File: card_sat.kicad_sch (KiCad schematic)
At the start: 24 parts, among them J1 Conn_01x05_Male, J2 Conn_01x05_Male, J3 Conn_01x05_Male, J4 Conn_01x05_Male, J5 Conn_01x04_Male, U1 ATtiny85-20P, U2 ATtiny85-20P, U3 ATtiny85-20P

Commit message: changed schematic to use pico
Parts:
- removed D1, D2: B340, symbol Diode:B340
- removed R10, R11: (no value), symbol Device:R
- removed U1, U2, U3: ATtiny85-20P, Package_DIP:DIP-8_W7.62mm, symbol MCU_Microchip_ATtiny:ATtiny85-20P
- added D1, D2: (no value), symbol Diode:1N5819
- added U1: (no value), symbol MCU_RaspberryPi_and_Boards:Pico
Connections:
- net +3V3: now also U1.36 (3V3)
- net +5V: now also D1.1 (K), D2.1 (K)
- net GND: now also U1.38 (GND)
- net PANEL1: now also D1.2 (A)
- net PANEL2: now also D2.2 (A)
- net RXD1: now also U1.4 (GPIO2); no longer J1.2 (Pin_2), J2.2 (Pin_2)
- net RXD2: now also U1.7 (GPIO5)
- net RXD3: now also U1.11 (GPIO8); no longer J3.2 (Pin_2), J4.2 (Pin_2)
- net RXD4: now also U1.15 (GPIO11)
- net at R4.2, R6.2: now also U1.24 (GPIO18)
- net at R8.2, R9.2: now also U1.26 (GPIO20)
- net at R5.2, R7.2: now also U1.25 (GPIO19)
- net SET2: now reaches J2.1 (Pin_1)
- net SET2: now also U1.5 (GPIO3)
- net SET4: now reaches J4.1 (Pin_1)
- net SET4: now also U1.12 (GPIO9)
- net SET1: now reaches J1.1 (Pin_1)
- net SET1: now also U1.1 (GPIO0)
- net SET3: now reaches J3.1 (Pin_1)
- net SET3: now also U1.9 (GPIO6)
- new net TXD1: J1.2 (Pin_2), U1.2 (GPIO1)
- new net TXD2: J2.2 (Pin_2), U1.6 (GPIO4)
- new net TXD3: J3.2 (Pin_2), U1.10 (GPIO7)
- new net TXD4: J4.2 (Pin_2), U1.14 (GPIO10)
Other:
- note removed: "+3.7v from Battery"

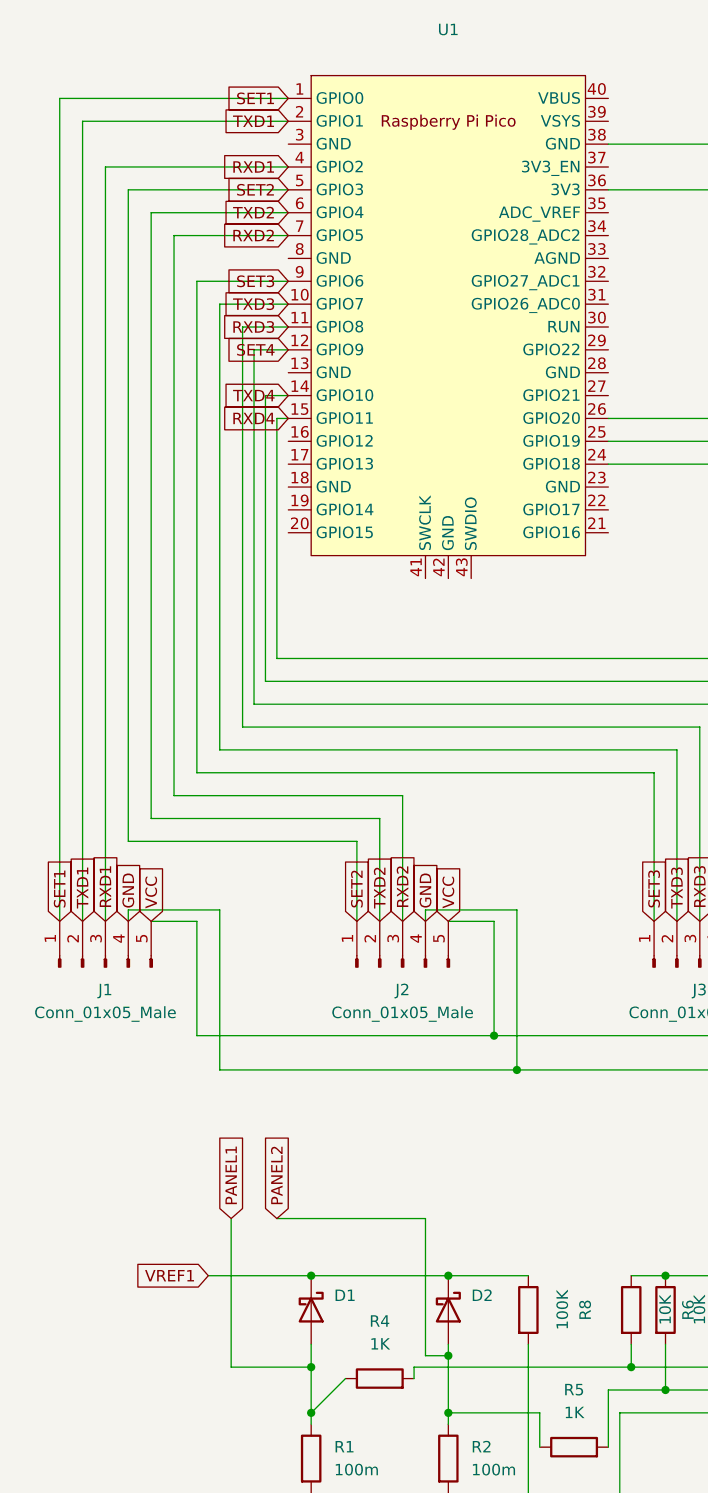
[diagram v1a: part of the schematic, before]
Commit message: switched to python
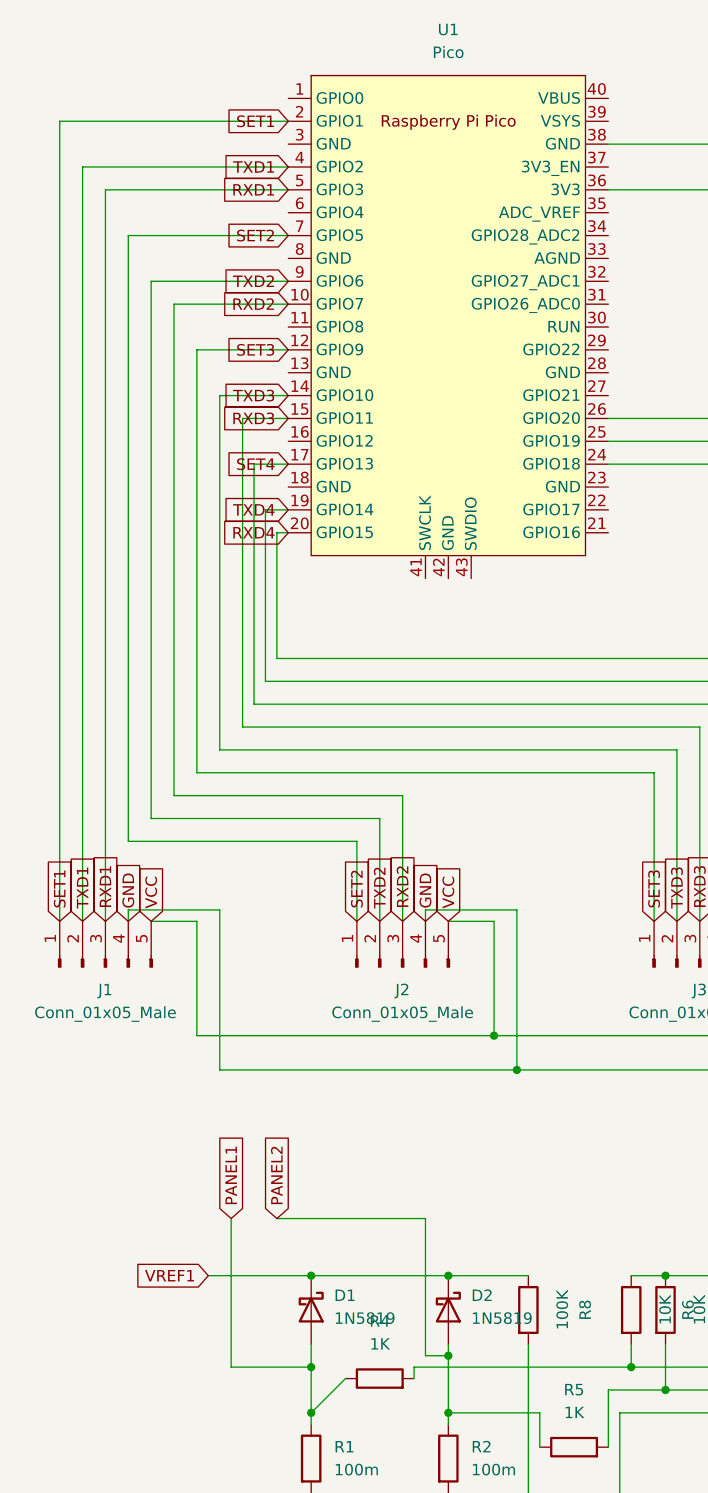
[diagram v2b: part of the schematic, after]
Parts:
- D1, D2: value (none) -> 1N5819; footprint (none) -> Diode_THT:D_DO-41_SOD81_P10.16mm_Horizontal
- U1: value (none) -> Pico; footprint (none) -> MCU_RaspberryPi_and_Boards:RPi_Pico_SMD_TH
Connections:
- net RXD1: now also U1.5 (GPIO3); no longer U1.4 (GPIO2)
- net RXD2: now also U1.10 (GPIO7); no longer U1.7 (GPIO5)
- net RXD3: now also U1.15 (GPIO11); no longer U1.11 (GPIO8)
- net RXD4: now also U1.20 (GPIO15); no longer U1.15 (GPIO11)
- net SET1: now also U1.2 (GPIO1); no longer U1.1 (GPIO0)
- net SET2: now also U1.7 (GPIO5); no longer U1.5 (GPIO3)
- net SET3: now also U1.12 (GPIO9); no longer U1.9 (GPIO6)
- net SET4: now also U1.17 (GPIO13); no longer U1.12 (GPIO9)
- net TXD1: now also U1.4 (GPIO2); no longer U1.2 (GPIO1)
- net TXD2: now also U1.9 (GPIO6); no longer U1.6 (GPIO4)
- net TXD3: now also U1.14 (GPIO10); no longer U1.10 (GPIO7)
- net TXD4: now also U1.19 (GPIO14); no longer U1.14 (GPIO10)

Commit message: debugging still :(
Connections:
- net at R4.2, R6.2: now also U1.31 (GPIO26_ADC0); no longer U1.24 (GPIO18)
- net at R8.2, R9.2: now also U1.34 (GPIO28_ADC2); no longer U1.26 (GPIO20)
- net at R5.2, R7.2: now also U1.32 (GPIO27_ADC1); no longer U1.25 (GPIO19)
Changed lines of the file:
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@@
+    (stroke (width 0) (type default) (color 0 0 0 0))
+  )
+  (wire (pts (xy 163.83 43.18) (xy 99.06 43.18))
     (stroke (width 0) (type default) (color 0 0 0 0))
   )
@@
     (stroke (width 0) (type default) (color 0 0 0 0))
   )
+  (wire (pts (xy 161.29 45.72) (xy 99.06 45.72))
+    (stroke (width 0) (type default) (color 0 0 0 0))
+  )
   (wire (pts (xy 101.6 163.83) (xy 161.29 163.83))
     (stroke (width 0) (type default) (color 0 0 0 0))
   )
-  (wire (pts (xy 166.37 168.91) (xy 166.37 58.42))
+  (wire (pts (xy 166.37 38.1) (xy 166.37 168.91))
     (stroke (width 0) (type default) (color 0 0 0 0))
   )
@@
     (stroke (width 0) (type default) (color 0 0 0 0))
   )
-  (wire (pts (xy 163.83 166.37) (xy 163.83 60.96))
+  (wire (pts (xy 163.83 43.18) (xy 163.83 166.37))
     (stroke (width 0) (type default) (color 0 0 0 0))
   )
@@
     (stroke (width 0) (type default) (color 0 0 0 0))
   )
-  (wire (pts (xy 166.37 58.42) (xy 99.06 58.42))
-    (stroke (width 0) (type default) (color 0 0 0 0))
-  )
   (wire (pts (xy 99.06 166.37) (xy 99.06 172.72))
     (stroke (width 0) (type default) (color 0 0 0 0))
@@
     (stroke (width 0) (type default) (color 0 0 0 0))
   )
+  (wire (pts (xy 99.06 38.1) (xy 166.37 38.1))
+    (stroke (width 0) (type default) (color 0 0 0 0))
+  )
   (wire (pts (xy 109.22 114.3) (xy 109.22 92.71))
     (stroke (width 0) (type default) (color 0 0 0 0))
@@
     (stroke (width 0) (type default) (color 0 0 0 0))
   )
-  (wire (pts (xy 161.29 63.5) (xy 99.06 63.5))
-    (stroke (width 0) (type default) (color 0 0 0 0))
-  )
   (wire (pts (xy 257.81 142.24) (xy 280.67 142.24))
     (stroke (width 0) (type default) (color 0 0 0 0))
@@
     (stroke (width 0) (type default) (color 0 0 0 0))
   )
-  (wire (pts (xy 161.29 163.83) (xy 161.29 63.5))
+  (wire (pts (xy 161.29 45.72) (xy 161.29 163.83))
     (stroke (width 0) (type default) (color 0 0 0 0))
   )
@@
     (stroke (width 0) (type default) (color 0 0 0 0))
   )
-  (wire (pts (xy 163.83 60.96) (xy 99.06 60.96))
-    (stroke (width 0) (type default) (color 0 0 0 0))
-  )
